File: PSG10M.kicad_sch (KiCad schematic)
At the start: 21 parts, among them SW1 RotaryEncoder_Switch, SW2 RotaryEncoder_Switch, U1 AD8933_module, U2 BluePill, U3 AD8606ARZ, U4 LMV331, U5 FSA3157L6X

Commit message: Ide nekako idk.
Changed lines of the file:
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@@
 		)
 		(instances
-			(project ""
+			(project "PSG10M"
 				(path "/60b34cbc-2eaa-4dea-9ec7-288b3cc4f4a7"
 					(reference "U3")
@@
 	)
 	(symbol
+		(lib_id "PSG:BluePill")
+		(at 179.07 71.12 0)
+		(unit 1)
+		(exclude_from_sim no)
+		(in_bom yes)
+		(on_board yes)
+		(dnp no)
+		(fields_autoplaced yes)
+		(property "Reference" "U2"
+			(at 179.07 40.64 0)
+			(effects
+				(font
+					(size 1.27 1.27)
+				)
+			)
+		)
+		(property "Value" "BluePill"
+			(at 179.07 43.18 0)
+			(effects
+				(font
+					(size 1.27 1.27)
+				)
+			)
+		)
+		(property "Footprint" "PSG:BluePill"
+			(at 199.39 96.52 0)
+			(effects
+				(font
+					(size 1.27 1.27)
+				)
+				(hide yes)
+			)
+		)
+		(property "Datasheet" ""
+			(at 199.39 96.52 0)
+			(effects
+				(font
+					(size 1.27 1.27)
+				)
+				(hide yes)
+			)
+		)
+		(property "Description" ""
+			(at 179.07 71.12 0)
+			(effects
+				(font
+					(size 1.27 1.27)
+				)
+				(hide yes)
+			)
+		)
+		(pin "8"
+		)
+		(pin "33"
+		)
+		(pin "39"
+		)
+		(pin "24"
+		)
+		(pin "36"
+		)
+		(pin "3"
+		)
+		(pin "15"
+		)
+		(pin "9"
+		)
+		(pin "32"
+		)
+		(pin "20"
+		)
+		(pin "26"
+		)
+		(pin "29"
+		)
+		(pin "21"
+		)
+		(pin "4"
+		)
+		(pin "2"
+		)
+		(pin "7"
+		)
+		(pin "41"
+		)
+		(pin "35"
+		)
+		(pin "11"
+		)
+		(pin "13"
+		)
+		(pin "14"
+		)
+		(pin "31"
+		)
+		(pin "10"
+		)
+		(pin "38"
+		)
+		(pin "23"
+		)
+		(pin "25"
+		)
+		(pin "17"
+		)
+		(pin "44"
+		)
+		(pin "1"
+		)
+		(pin "22"
+		)
+		(pin "30"
+		)
+		(pin "19"
+		)
+		(pin "5"
+		)
+		(pin "6"
+		)
+		(pin "43"
+		)
+		(pin "12"
+		)
+		(pin "28"
+		)
+		(pin "18"
+		)
+		(pin "40"
+		)
+		(pin "42"
+		)
+		(pin "34"
+		)
+		(pin "16"
+		)
+		(pin "27"
+		)
+		(pin "37"
+		)
+		(instances
+			(project "PSG10M"
+				(path "/60b34cbc-2eaa-4dea-9ec7-288b3cc4f4a7"
+					(reference "U2")
+					(unit 1)
+				)
+			)
+		)
+	)
+	(symbol
 		(lib_id "Device:R_Potentiometer")
 		(at 109.22 238.76 0)
@@
 		)
 		(instances
-			(project ""
+			(project "PSG10M"
 				(path "/60b34cbc-2eaa-4dea-9ec7-288b3cc4f4a7"
 					(reference "#PWR05")
@@
 	)
 	(symbol
-		(lib_id "PSG:BluePill")
-		(at 193.04 72.39 0)
-		(unit 1)
-		(exclude_from_sim no)
-		(in_bom yes)
-		(on_board yes)
-		(dnp no)
-		(fields_autoplaced yes)
-		(property "Reference" "U2"
-			(at 193.04 41.91 0)
-			(effects
-				(font
-					(size 1.27 1.27)
-				)
-			)
-		)
-		(property "Value" "BluePill"
-			(at 193.04 44.45 0)
-			(effects
-				(font
-					(size 1.27 1.27)
-				)
-			)
-		)
-		(property "Footprint" "PSG:BluePill"
-			(at 213.36 97.79 0)
-			(effects
-				(font
-					(size 1.27 1.27)
-				)
-				(hide yes)
-			)
-		)
-		(property "Datasheet" ""
-			(at 213.36 97.79 0)
-			(effects
-				(font
-					(size 1.27 1.27)
-				)
-				(hide yes)
-			)
-		)
-		(property "Description" ""
-			(at 193.04 72.39 0)
-			(effects
-				(font
-					(size 1.27 1.27)
-				)
-				(hide yes)
-			)
-		)
-		(pin "19"
-		)
-		(pin "2"
-		)
-		(pin "20"
-		)
-		(pin "15"
-		)
-		(pin "13"
-		)
-		(pin "22"
-		)
-		(pin "23"
-		)
-		(pin "24"
-		)
-		(pin "12"
-		)
-		(pin "25"
-		)
-		(pin "26"
-		)
-		(pin "21"
-		)
-		(pin "14"
-		)
-		(pin "1"
-		)
-		(pin "16"
-		)
-		(pin "10"
-		)
-		(pin "11"
-		)
-		(pin "17"
-		)
-		(pin "18"
-		)
-		(pin "27"
-		)
-		(pin "28"
-		)
-		(pin "30"
-		)
-		(pin "33"
-		)
-		(pin "34"
-		)
-		(pin "38"
-		)
-		(pin "3"
-		)
-		(pin "35"
-		)
-		(pin "4"
-		)
-		(pin "7"
-		)
-		(pin "36"
-		)
-		(pin "31"
-		)
-		(pin "44"
-		)
-		(pin "41"
-		)
-		(pin "9"
-		)
-		(pin "39"
-		)
-		(pin "32"
-		)
-		(pin "37"
-		)
-		(pin "40"
-		)
-		(pin "8"
-		)
-		(pin "5"
-		)
-		(pin "42"
-		)
-		(pin "6"
-		)
-		(pin "29"
-		)
-		(pin "43"
-		)
-		(instances
-			(project ""
-				(path "/60b34cbc-2eaa-4dea-9ec7-288b3cc4f4a7"
-					(reference "U2")
-					(unit 1)
-				)
-			)
-		)
-	)
-	(symbol
 		(lib_id "power:GND")
 		(at 109.22 254 0)
@@
 		)
 		(instances
-			(project ""
+			(project "PSG10M"
 				(path "/60b34cbc-2eaa-4dea-9ec7-288b3cc4f4a7"
 					(reference "R1")
@@
 		)
 		(instances
-			(project ""
+			(project "PSG10M"
 				(path "/60b34cbc-2eaa-4dea-9ec7-288b3cc4f4a7"
 					(reference "RV1")
@@
 		)
 		(instances
-			(project ""
+			(project "PSG10M"
 				(path "/60b34cbc-2eaa-4dea-9ec7-288b3cc4f4a7"
 					(reference "U1")
@@
 		)
 		(instances
-			(project ""
+			(project "PSG10M"
 				(path "/60b34cbc-2eaa-4dea-9ec7-288b3cc4f4a7"
 					(reference "SW1")
@@
 		)
 		(instances
-			(project ""
+			(project "PSG10M"
 				(path "/60b34cbc-2eaa-4dea-9ec7-288b3cc4f4a7"
 					(reference "U3")

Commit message: Ids
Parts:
- removed R10, R9: 100k, Resistor_SMD:R_0603_1608Metric_Pad0.98x0.95mm_HandSolder, symbol Device:R_US
- removed R7: 1k, Resistor_SMD:R_0603_1608Metric_Pad0.98x0.95mm_HandSolder, symbol Device:R_US
- removed R8: 2k, Resistor_SMD:R_0603_1608Metric_Pad0.98x0.95mm_HandSolder, symbol Device:R_US
- removed RV2: 5k, symbol Device:R_Potentiometer
- removed U3: AD8606ARZ, Package_SO:SOIC-8_3.9x4.9mm_P1.27mm, symbol Amplifier_Operational:AD8606ARZ
- removed U4: LMV331, Package_TO_SOT_SMD:SOT-23-5_HandSoldering, symbol Comparator:LMV331
- added C1, C2, C3, C4, C5: 100n, Capacitor_SMD:C_0603_1608Metric_Pad1.08x0.95mm_HandSolder, symbol Device:C
- added R14: 33k, Resistor_SMD:R_0603_1608Metric_Pad0.98x0.95mm_HandSolder, symbol Device:R_US
- added R15: 50, Resistor_SMD:R_0603_1608Metric_Pad0.98x0.95mm_HandSolder, symbol Device:R_US
- added U3: FSA3157L6X, Package_TO_SOT_SMD:SOT-363_SC-70-6, symbol Analog_Switch:FSA3157L6X
- added U6: AD8039, Package_SO:SOIC-8_3.9x4.9mm_P1.27mm, symbol PSG:AD8039
- added U7: LM393LVDDFR, Package_TO_SOT_SMD:SOT-223-8, symbol PSG:LM393LVDDFR
- R11: value 1k -> 10k
- R12: value 2k -> 10k
- RV1: value 5k -> 50k
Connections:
- net +3V3: now also C1.1, R15.2
- net GND: now also R11.1, C1.2, C2.2, C3.2, C4.2, C5.2, U7.4 (V-)
- net PWM_DAC: now also U7.3 (+)
- net at R12.2: now also R14.1; no longer U5.3
- net at U5.1: now also R15.1, U7.1
- net at R11.2, R12.1: now also U6.2 (-)
- net at R1.2, R4.2: now also U6.5 (+)
- net at R2.1, R3.2: now also U6.6 (-)
- net at R2.2: now also U6.7
- net at U1.7 (OUT): now also U3.3, U6.3 (+)
- net at R1.1: now also U3.4; no longer U5.4
- net at R3.1, RV1.2: now also C4.1
- net +5V: now reaches U1.1 (V_{cc})
- net +5V: now also C2.1, C5.1, U6.8 (V+), U7.8 (V+)
- new net: R14.2, U5.3, U6.1, U7.2 (-)
- new net: U3.1, U5.4
- new net -5V: C3.1, U6.4 (V-)
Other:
- note added: "MOŽDA 8 channel mux"
- note removed: "MOVE to 0V to 3.3V space"
- moved on the sheet: R1, R11, R12, R2, R3, R4, R5, R6, RV1, U1, U5A

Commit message: JFET-added
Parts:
- removed SW1, SW2: RotaryEncoder_Switch, Rotary_Encoder:RotaryEncoder_Bourns_Vertical_PEC12R-3x17F-Sxxxx, symbol Device:RotaryEncoder_Switch
- removed U2: BluePill, PSG:BluePill, symbol PSG:BluePill
- added Q1: 2N3819, Package_TO_SOT_THT:TO-92, symbol Transistor_FET:2N3819
- added Q2: MMBF4393, Package_TO_SOT_SMD:SOT-23, symbol Transistor_FET:MMBF4393
- added R7, R8: 100k, Resistor_SMD:R_0603_1608Metric_Pad0.98x0.95mm_HandSolder, symbol Device:R_US
- added R9: 100, Resistor_SMD:R_0603_1608Metric_Pad0.98x0.95mm_HandSolder, symbol Device:R_US
- added U4: AD8039, Package_SO:SOIC-8_3.9x4.9mm_P1.27mm, symbol PSG:AD8039
- R2, R4: value 2k -> 2.2k
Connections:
- net GND: now also Q1.3 (S), Q2.2 (S)
- net at U3.4: now also U4.3 (+); no longer R1.1
- new net: R9.1, U4.1, U4.2 (-)
- new net: Q1.1 (D), Q2.1 (D), R7.2, R9.2, U4.5 (+)
- new net: Q1.2 (G), Q2.3 (G), R7.1, R8.1
- new net: R1.1, U4.6 (-), U4.7
- new net GAIN_SET_DAC: R8.2
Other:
- added sheet MCU (mcu.kicad_sch)
- moved on the sheet: C1, C2, C3, C4, C5, R1, R11, R12, R14, R15, R2, R3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

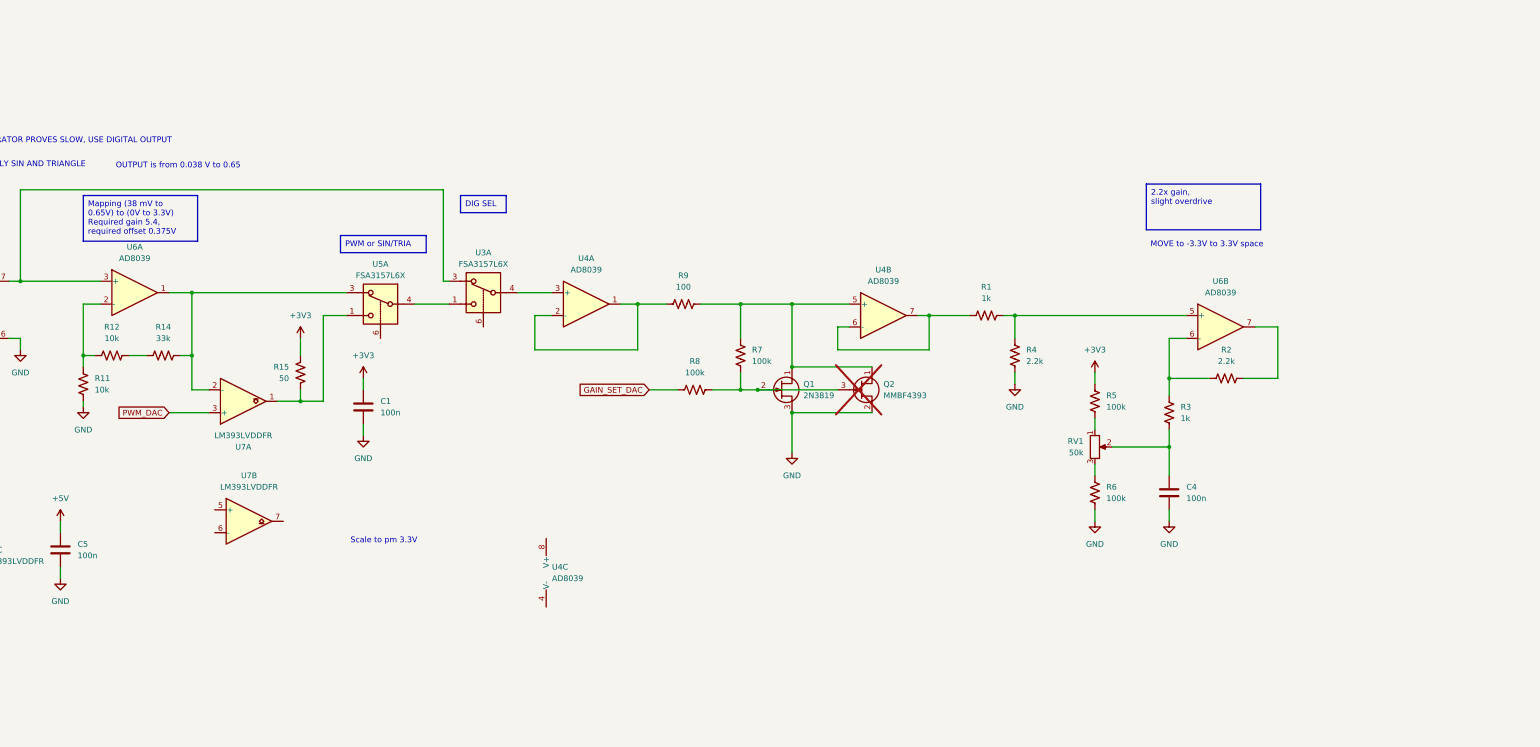
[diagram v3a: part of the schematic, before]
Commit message: Added DC offset, specifics TBD
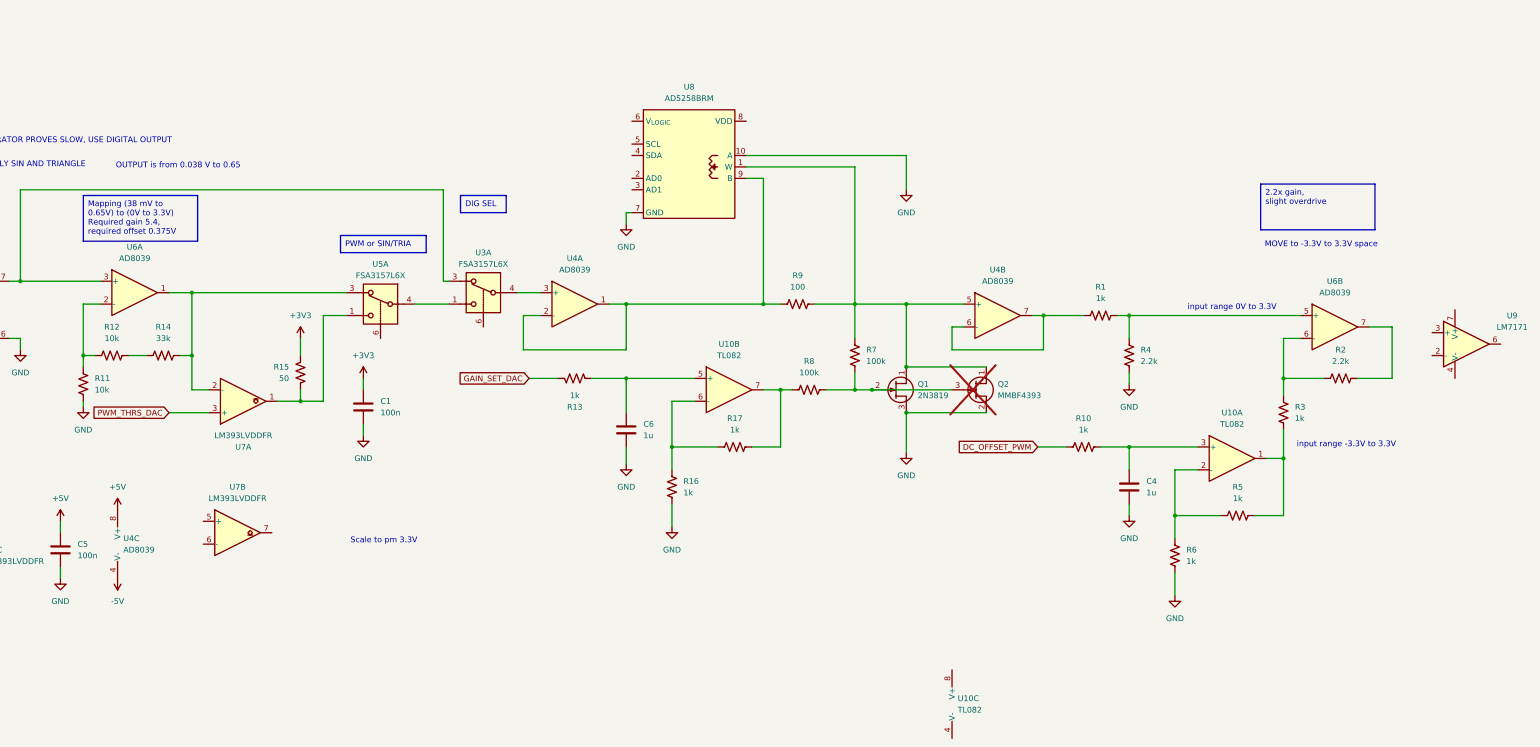
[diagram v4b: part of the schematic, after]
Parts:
- removed RV1: 50k, symbol Device:R_Potentiometer
- added C6: 1u, symbol Device:C
- added R10, R13, R16, R17: 1k, Resistor_SMD:R_0603_1608Metric_Pad0.98x0.95mm_HandSolder, symbol Device:R_US
- added U10: TL082, symbol Amplifier_Operational:TL082
- added U8: AD5258BRM, Package_SO:MSOP-10_3x3mm_P0.5mm, symbol PSG:AD5258BRM
- added U9: LM7171, Package_SO:SOIC-8_3.9x4.9mm_P1.27mm, symbol PSG:LM7171
- C4: value 100n -> 1u; footprint Capacitor_SMD:C_0603_1608Metric_Pad1.08x0.95mm_HandSolder -> (none)
- R5, R6: value 100k -> 1k
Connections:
- net +3V3: no longer R5.2
- net +5V: now also U4.8 (V+)
- net -5V: now also U4.4 (V-)
- net GAIN_SET_DAC: now also R13.1; no longer R8.2
- net GND: now also C6.2, R16.1, U8.10 (A), U8.7 (GND)
- net at R6.2: now also R5.1, U10.2 (-)
- net at R9.1, U4.1, U4.2 (-): now also U8.9 (B)
- net at Q1.1 (D), Q2.1 (D), R7.2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: now also U8.1 (W)
- net at C4.1: now also R10.2, U10.3 (+); no longer R3.1
- net PWM_DAC renamed PWM_THRS_DAC
- new net: C6.1, R13.2, U10.5 (+)
- new net: R16.2, R17.1, U10.6 (-)
- new net: R17.2, R8.2, U10.7
- new net: R3.1, R5.2, U10.1
- new net DC_OFFSET_PWM: R10.1
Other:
- note added: "input range -3.3V to 3.3V"
- note added: "input range 0V to 3.3V"
- moved on the sheet: Q1, Q2, R1, R2, R3, R4, R7, R8, R9, U4A, U4B, U4C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

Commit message: Save game. Power supply next.
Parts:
- added J1: Conn_Coaxial, Connector_Coaxial:BNC_Amphenol_B6252HB-NPP3G-50_Horizontal, symbol Connector:Conn_Coaxial
- added R18: 2k, Resistor_SMD:R_0603_1608Metric_Pad0.98x0.95mm_HandSolder, symbol Device:R_US
- added R19: 1k, Resistor_SMD:R_0603_1608Metric_Pad0.98x0.95mm_HandSolder, symbol Device:R_US
- added R20: 50, Resistor_SMD:R_0603_1608Metric_Pad0.98x0.95mm_HandSolder, symbol Device:R_US
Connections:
- net GND: now also J1.2 (Ext), R19.1
- net at R2.2, U6.7: now also U9.3 (+)
- net OUT_3V3: now reaches R9.1, U4.1, U4.2 (-), U8.9 (B)
- net at U9.2 (-): now also R18.1, R19.2
- net -15V: now reaches U9.4 (V-)
- net at U9.6: now also R18.2, R20.1
- net +15V: now reaches U9.7 (V+)
- new net: J1.1 (In), R20.2
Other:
- note added: "MORA BITI 15V"
- moved on the sheet: C1, C2, C3, C4, C5, C6, Q1, Q2, R1, R10, R11, R12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

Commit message: Working on PSY. Oddball values are fun.
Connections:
- net +15V renamed +16.5V
- net -15V renamed -16.5V
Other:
- added sheet PSU (psu.kicad_sch)
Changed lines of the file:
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@@
 			)
 		)
-		(property "Value" "+15V"
+		(property "Value" "+16.5V"
 			(at 254 201.93 0)
 			(effects
@@
 			)
 		)
-		(property "Value" "-15V"
+		(property "Value" "-16.5V"
 			(at 254 227.33 0)
 			(effects
@@
 				)
 			)
+		)
+	)
+	(sheet
+		(at 17.78 78.74)
+		(size 27.94 22.86)
+		(fields_autoplaced yes)
+		(stroke
+			(width 0.1524)
+			(type solid)
+		)
+		(fill
+			(color 0 194 194 1.0000)
+		)
+		(property "Sheetname" "PSU"
+			(at 17.78 78.0284 0)
+			(effects
+				(font
+					(size 1.27 1.27)
+				)
+				(justify left bottom)
+			)
+		)
+		(property "Sheetfile" "psu.kicad_sch"
+			(at 17.78 102.1846 0)
+			(effects
+				(font
+					(size 1.27 1.27)
+				)
+				(justify left top)
+			)
+		)
+		(pin "GAIN_SET_DAC" output
+			(at 45.72 81.28 0)
+			(effects
+				(font
+					(size 1.27 1.27)
+					(color 0 0 0 1)
+				)
+				(justify right)
+			)
+		)
+		(instances
+			(project "PSG10M"
+				(path "/60b34cbc-2eaa-4dea-9ec7-288b3cc4f4a7"
+					(page "3")
+				)
+			)

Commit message: Progress.
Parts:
- removed C1, C2, C3, C5: 100n, Capacitor_SMD:C_0603_1608Metric_Pad1.08x0.95mm_HandSolder, symbol Device:C
- removed C4, C6: 1u, symbol Device:C
- removed J1: Conn_Coaxial, Connector_Coaxial:BNC_Amphenol_B6252HB-NPP3G-50_Horizontal, symbol Connector:Conn_Coaxial
- removed Q1: 2N3819, Package_TO_SOT_THT:TO-92, symbol Transistor_FET:2N3819
- removed Q2: MMBF4393, Package_TO_SOT_SMD:SOT-23, symbol Transistor_FET:MMBF4393
- removed R1, R10, R13, R16, R17, R19, R3, R5, R6: 1k, Resistor_SMD:R_0603_1608Metric_Pad0.98x0.95mm_HandSolder, symbol Device:R_US
- removed R11, R12: 10k, Resistor_SMD:R_0603_1608Metric_Pad0.98x0.95mm_HandSolder, symbol Device:R_US
- removed R14: 33k, Resistor_SMD:R_0603_1608Metric_Pad0.98x0.95mm_HandSolder, symbol Device:R_US
- removed R15, R20: 50, Resistor_SMD:R_0603_1608Metric_Pad0.98x0.95mm_HandSolder, symbol Device:R_US
- removed R18: 2k, Resistor_SMD:R_0603_1608Metric_Pad0.98x0.95mm_HandSolder, symbol Device:R_US
- removed R2, R4: 2.2k, Resistor_SMD:R_0603_1608Metric_Pad0.98x0.95mm_HandSolder, symbol Device:R_US
- removed R7, R8: 100k, Resistor_SMD:R_0603_1608Metric_Pad0.98x0.95mm_HandSolder, symbol Device:R_US
- removed R9: 100, Resistor_SMD:R_0603_1608Metric_Pad0.98x0.95mm_HandSolder, symbol Device:R_US
- removed U1: AD8933_module, PSG:AD9833_module, symbol PSG:AD8933_module
- removed U10: TL082, symbol Amplifier_Operational:TL082
- removed U3, U5: FSA3157L6X, Package_TO_SOT_SMD:SOT-363_SC-70-6, symbol Analog_Switch:FSA3157L6X
- removed U4, U6: AD8039, Package_SO:SOIC-8_3.9x4.9mm_P1.27mm, symbol PSG:AD8039
- removed U7: LM393LVDDFR, Package_TO_SOT_SMD:SOT-223-8, symbol PSG:LM393LVDDFR
- removed U8: AD5258BRM, Package_SO:MSOP-10_3x3mm_P0.5mm, symbol PSG:AD5258BRM
- removed U9: LM7171, Package_SO:SOIC-8_3.9x4.9mm_P1.27mm, symbol PSG:LM7171
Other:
- added sheet AMP (amp.kicad_sch)
- sheet MCU ports: added DC_OFFSET_PWM, PWM_SEL, PWM_THRS_DAC, SQUARE_SEL; removed none
- sheet PSU ports: added none; removed GAIN_SET_DAC
- note removed: "MORA BITI 15V"
- note removed: "MOVE to -3.3V to 3.3V space"
- note removed: "Scale to pm 3.3V"
- note removed: "input range -3.3V to 3.3V"
- note removed: "input range 0V to 3.3V"

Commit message: Savegame.
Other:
- sheet AMP ports: added FSYNC_SG, SCK_SG, SDATA_SG; removed none
- sheet MCU ports: added FSYNC_SG, SCK_SG, SDATA_SG; removed none
